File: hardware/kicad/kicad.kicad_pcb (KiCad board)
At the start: 2 copper layers, 272 x 197 mm, 107 parts, among them J1 Conn_01x13_Female, SW0 MX_SW, SW1 MX_SW, SW10 MX_SW, SW11 MX_SW, SW12 MX_SW, SW13 MX_SW, SW14 MX_SW, SW15 MX_SW, SW16 MX_SW, SW17 MX_SW, SW18 MX_SW, SW19 MX_SW, SW2 MX_SW, SW20 MX_SW, SW21 MX_SW, SW22 MX_SW, SW23 MX_SW, SW24 MX_SW, SW25 MX_SW, SW26 MX_SW, SW27 MX_SW, SW28 MX_SW, SW29 MX_SW, SW3 MX_SW, SW30 MX_SW, SW31 MX_SW, SW4 MX_SW, SW5 MX_SW, SW6 MX_SW, SW7 MX_SW, SW8 MX_SW, SW9 MX_SW, U1 Pico, U2 MC74HC589ADR2G, U3 MC74HC589ADR2G, U4 MC74HC589ADR2G, U5 MC74HC589ADR2G, U6 ILI9163, U7 ILI9341_TS

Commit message: Matrix wired
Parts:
- removed LED29, LED30, LED31: MX_SK6812MINI-E, marbastlib-mx:LED_MX_6028R
- removed R29, R30, R31: R_Small, Resistor_SMD:R_1206_3216Metric_Pad1.30x1.75mm_HandSolder
- removed SW29, SW30, SW31: MX_SW, marbastlib-mx:SW_MX_1u
- removed U2, U3, U4, U5: MC74HC589ADR2G, Package_SO:SO-16_3.9x9.9mm_P1.27mm
- added UROW1: MC74HC589ADR2G, Package_SO:SO-16_3.9x9.9mm_P1.27mm, F.Cu at (289.0, 54.0)
- added UROW2: MC74HC589ADR2G, Package_SO:SO-16_3.9x9.9mm_P1.27mm, F.Cu at (289.0, 73.7)
- added UROW3: MC74HC589ADR2G, Package_SO:SO-16_3.9x9.9mm_P1.27mm, F.Cu at (289.0, 92.0)
- added UROW4: MC74HC589ADR2G, Package_SO:SO-16_3.9x9.9mm_P1.27mm, F.Cu at (289.0, 111.0)
- added UROW5: MC74HC589ADR2G, Package_SO:SO-16_3.9x9.9mm_P1.27mm, F.Cu at (289.0, 131.0)
- moved U6 89.9 mm to (314.1, 199.4)
- moved U1 59.4 mm to (331.0, 67.0)
- moved U7 37.0 mm to (206.1, 143.2)
- moved USIPO0 33.9 mm to (326.0, 142.0)
- moved USIPO1 33.9 mm to (342.0, 142.0)
- moved USIPO2 33.9 mm to (358.0, 142.0)
- moved R6 23.2 mm to (278.0, 65.8), turned to 0 degrees
- moved R11 21.8 mm to (278.0, 80.8), turned to 0 degrees
- moved R24 20.1 mm to (278.0, 123.5), turned to 0 degrees
- moved R16 20.0 mm to (278.0, 96.8), turned to 0 degrees
- moved R10 9.80 mm to (278.0, 77.8)
- moved R18 8.80 mm to (278.0, 103.0)
- moved R20 8.80 mm to (278.0, 109.0)
- moved R23 8.80 mm to (278.0, 118.0)
- moved R19 8.80 mm to (278.0, 106.0)
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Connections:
- net Net-(LED15-Pad2) renamed RGB15_OUT
- net Net-(LED23-Pad2) renamed RGB23_OUT
- net Net-(LED7-Pad2) renamed RGB7_OUT
- LED28 pad 2: Net-(LED28-Pad2) -> unconnected-(LED28-Pad2)
- SW16 pad 1: +3V3 -> Net-(SW16-Pad1)
- SW17 pad 1: +3V3 -> Net-(SW16-Pad1)
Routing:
- net Net-(R17-Pad2): track 0.00 -> 140.4 mm, vias 0 -> 1
- net Net-(R23-Pad2): track 0.00 -> 140.2 mm, vias 0 -> 1
- net Net-(R28-Pad2): track 0.00 -> 138.0 mm, vias 0 -> 1
- net Net-(LED5-Pad2): track 0.00 -> 118.7 mm, vias 0 -> 2
- net Net-(LED17-Pad2): track 0.00 -> 118.5 mm, vias 0 -> 2
- net Net-(LED11-Pad2): track 0.00 -> 118.5 mm, vias 0 -> 2
- net Net-(R22-Pad2): track 0.00 -> 118.2 mm, vias 0 -> 1
- net Net-(R16-Pad2): track 0.00 -> 117.8 mm, vias 0 -> 1
- net Net-(R27-Pad2): track 0.00 -> 115.3 mm, vias 0 -> 1
- net PISO_CS: track 0.00 -> 110.7 mm, vias 0 -> 5
- net RGB23_OUT: track 0.00 -> 110.5 mm, vias 0 -> 2
- net REGISTER_SCK: track 0.00 -> 98.1 mm, vias 0 -> 5
- net Net-(R21-Pad2): track 0.00 -> 95.8 mm, vias 0 -> 1
- net Net-(R15-Pad2): track 0.00 -> 95.6 mm, vias 0 -> 1
- net PISO_LATCH: track 0.00 -> 94.9 mm
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- added copper zone on B.Cu, net +3V3
- added copper zone on F.Cu, net GND

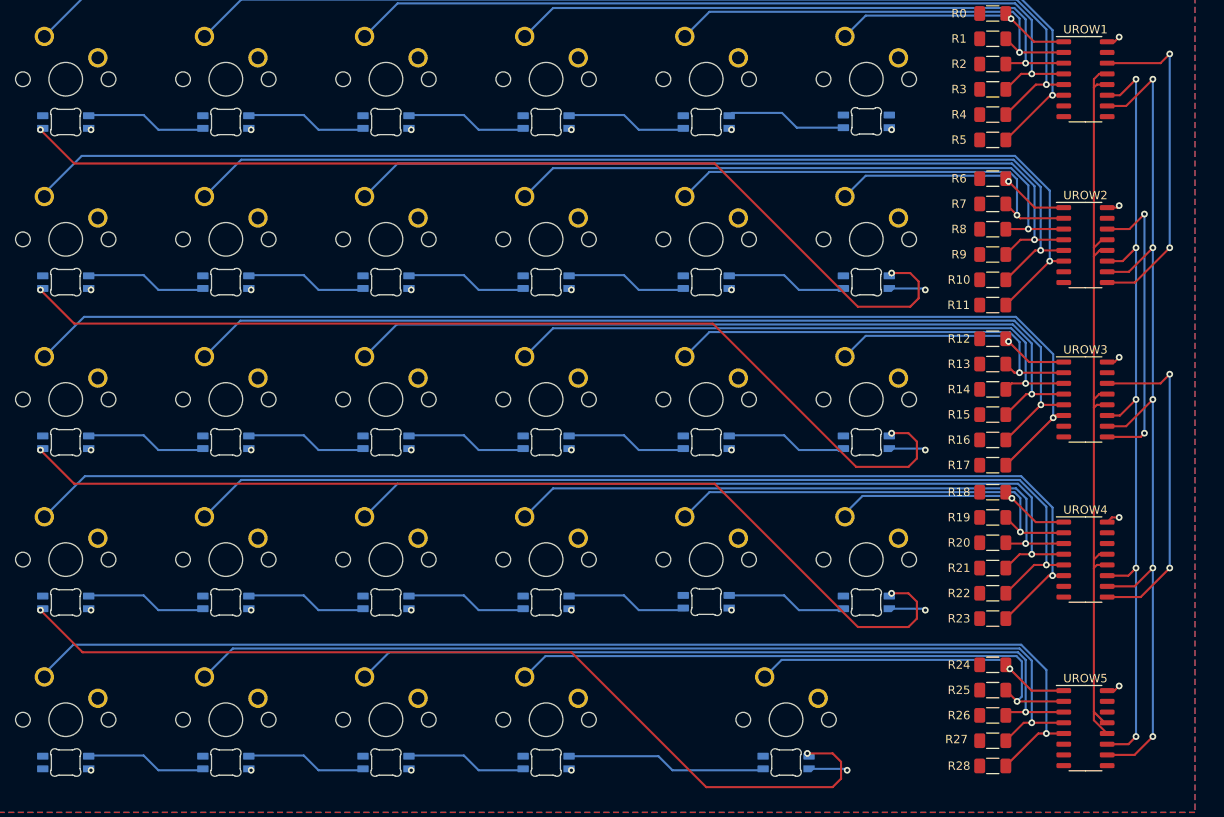
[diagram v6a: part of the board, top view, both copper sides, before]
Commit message: Add missing row5 to row4 chain
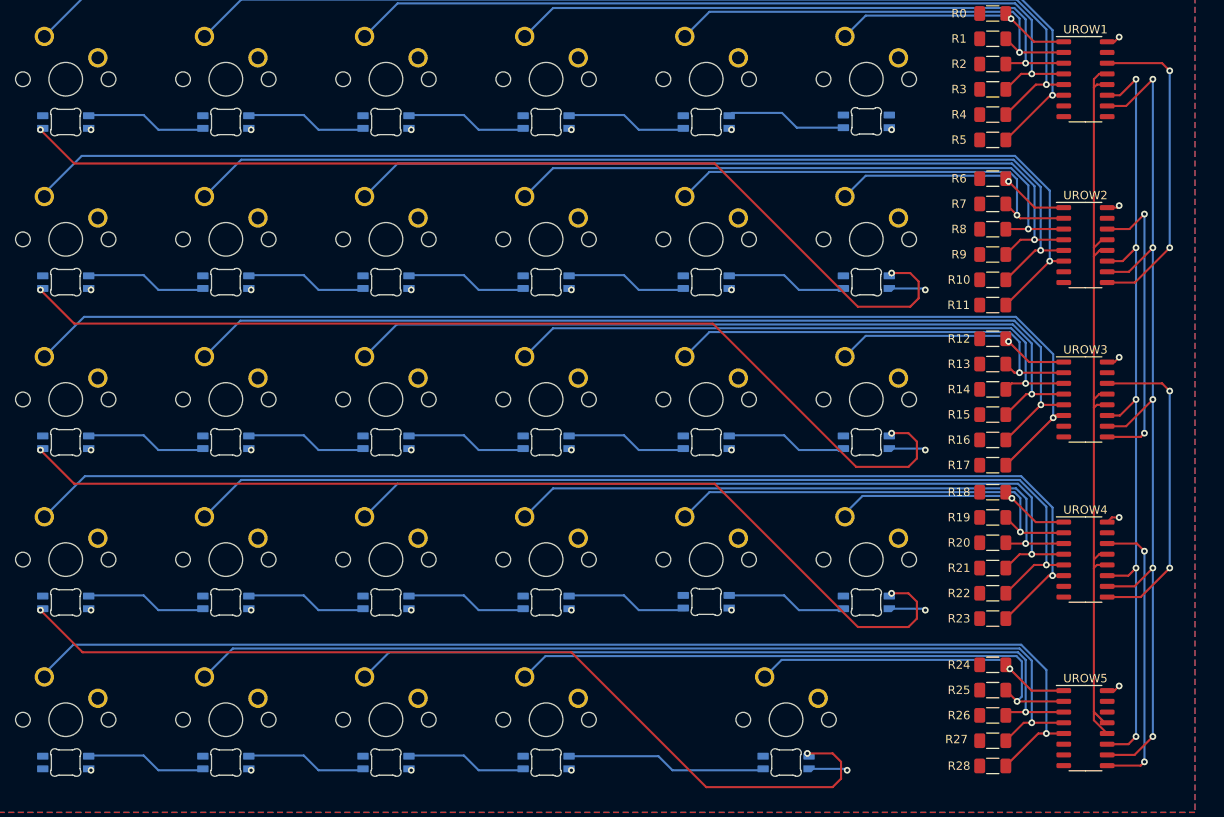
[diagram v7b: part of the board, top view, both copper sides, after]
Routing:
- net ROW5_OUT: track 0.00 -> 34.4 mm, vias 0 -> 2
- net ROW4_OUT: track 39.7 -> 37.7 mm
- net ROW2_OUT: track 40.0 -> 37.9 mm
